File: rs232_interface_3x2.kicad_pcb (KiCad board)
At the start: 2 copper layers, 70.5 x 41.9 mm, 9 parts, among them J1 DB9M_RA, U1 RS232_2x2

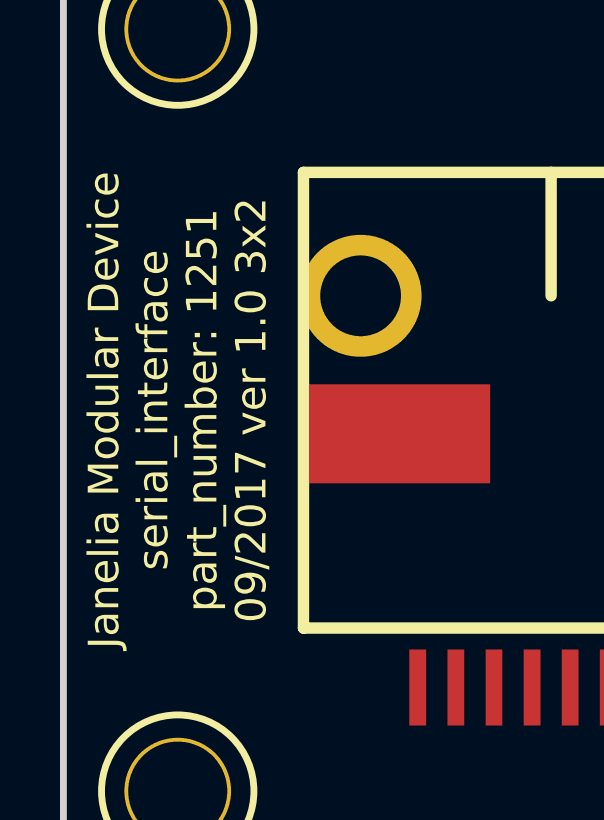
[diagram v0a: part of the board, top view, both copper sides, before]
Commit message: serial -> rs232.
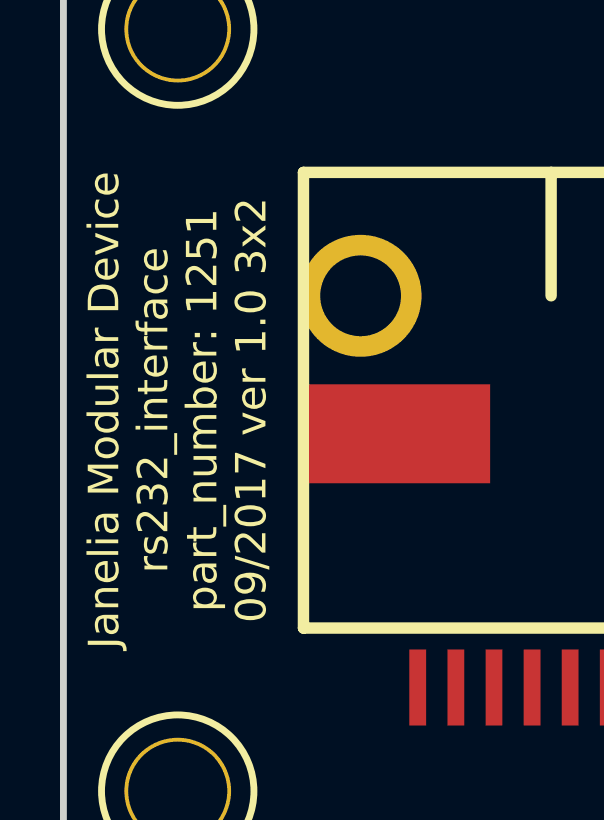
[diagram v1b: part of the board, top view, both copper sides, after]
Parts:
- C1, C2, C3, C4, C5: footprint serial_interface_3x2:SM1210 -> rs232_interface_3x2:SM1210
- J1: footprint serial_interface_3x2:DB9M_RA -> rs232_interface_3x2:DB9M_RA
- MDB1: footprint serial_interface_3x2:MODULAR_DEVICE_BASE_3X2_MALE -> rs232_interface_3x2:MODULAR_DEVICE_BASE_3X2_MALE
- RJ1: footprint serial_interface_3x2:RJ45_8P8C_2PORT_1ROW_RA_SMD -> rs232_interface_3x2:RJ45_8P8C_2PORT_1ROW_RA_SMD
- U1: footprint serial_interface_3x2:SOIC_16 -> rs232_interface_3x2:SOIC_16
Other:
- board text added: "Janelia Modular Device rs232_interface part_number: 1251 09/2017 ver 1.0 3x2"
- board text removed: "Janelia Modular Device serial_interface part_number: 1251 09/2017 ver 1.0 3x2"
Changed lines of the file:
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@@
   (page A4)
   (title_block
-    (title serial_interface_3x2)
+    (title rs232_interface_3x2)
     (rev 1.0)
   )
@@
     (diff_pair_width 0.254)
   )
-  (module serial_interface_3x2:DB9M_RA (layer F.Cu)
+  (module rs232_interface_3x2:DB9M_RA (layer F.Cu)
     (at 146.685 88.9 90)
     (fp_text reference J1 (at 0 -3.81 90) (layer F.SilkS)
@@
     (pad 9 thru_hole oval (at 4.155 1.42 90) (size 1.6 2.2) (drill 1) (layers *.Cu *.Mask))
   )
-  (module serial_interface_3x2:SOIC_16 (layer B.Cu)
+  (module rs232_interface_3x2:SOIC_16 (layer B.Cu)
     (at 134.62 88.9)
     (solder_mask_margin 0.1016)
@@
       (net 2 "Net-(C1-Pad1)"))
   )
-  (module serial_interface_3x2:MODULAR_DEVICE_BASE_3X2_MALE (layer F.Cu)
+  (module rs232_interface_3x2:MODULAR_DEVICE_BASE_3X2_MALE (layer F.Cu)
     (at 107.315 88.9)
     (fp_text reference MDB1 (at 0 0) (layer F.SilkS) hide
@@
       (net 6 GND))
   )
-  (module serial_interface_3x2:SM1210 (layer F.Cu)
+  (module rs232_interface_3x2:SM1210 (layer F.Cu)
     (at 169.181802 91.811719)
     (tags "CMS SM")
@@
     )
   )
-  (module serial_interface_3x2:SM1210 (layer F.Cu)
+  (module rs232_interface_3x2:SM1210 (layer F.Cu)
     (at 200.871802 85.101719)
     (tags "CMS SM")
@@
     )
   )
-  (module serial_interface_3x2:SM1210 (layer F.Cu)
+  (module rs232_interface_3x2:SM1210 (layer F.Cu)
     (at 174.381802 91.811719)
     (tags "CMS SM")
@@
     )
   )
-  (module serial_interface_3x2:SM1210 (layer F.Cu)
+  (module rs232_interface_3x2:SM1210 (layer F.Cu)
     (at 213.061802 70.911719)
     (tags "CMS SM")
@@
     )
   )
-  (module serial_interface_3x2:SM1210 (layer F.Cu)
+  (module rs232_interface_3x2:SM1210 (layer F.Cu)
     (at 179.581802 91.811719)
     (tags "CMS SM")
@@
     )
   )
-  (module serial_interface_3x2:RJ45_8P8C_2PORT_1ROW_RA_SMD (layer F.Cu)
+  (module rs232_interface_3x2:RJ45_8P8C_2PORT_1ROW_RA_SMD (layer F.Cu)
     (at 109.855 85.09 180)
     (fp_text reference RJ1 (at 0 -12.065 180) (layer F.SilkS)
@@
     (effects (font (size 1.016 1.016) (thickness 0.1905)))
   )
-  (gr_text "Janelia Modular Device\nserial_interface\npart_number: 1251\n09/2017 ver 1.0 3x2" (at 89.535 88.9 90) (layer F.SilkS)
+  (gr_text "Janelia Modular Device\nrs232_interface\npart_number: 1251\n09/2017 ver 1.0 3x2" (at 89.535 88.9 90) (layer F.SilkS)
     (effects (font (size 1.016 1.016) (thickness 0.254)))
   )

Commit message: Progress towards v1.0.
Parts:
- removed RJ1: RJ45_8P8C_2PORT_1ROW_RA_SMD, rs232_interface_3x2:RJ45_8P8C_2PORT_1ROW_RA_SMD
- added J2: DB9F, rs232_interface_3x2:DB9F, F.Cu at (109.9, 96.5)
- C1, C2, C3, C4, C5: moved to B.Cu
- J1: value DB9M_RA -> DB9M; footprint rs232_interface_3x2:DB9M_RA -> rs232_interface_3x2:DB9M
- moved C4 71.7 mm to (146.1, 96.5), turned to 270 degrees
- moved C2 55.2 mm to (146.1, 91.4), turned to 270 degrees
- moved C5 53.0 mm to (127.0, 85.1), turned to 270 degrees
- moved J1 37.6 mm to (109.9, 81.3), turned to 0 degrees
- moved C3 30.2 mm to (146.1, 81.3), turned to 90 degrees
- moved C1 23.8 mm to (146.1, 86.4), turned to 270 degrees
- moved U1 2.01 mm to (136.5, 88.3), turned to 180 degrees
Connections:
- net /RD renamed /RXD
- net /TD renamed /TXD
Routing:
- net GND: track 0.00 -> 110.0 mm
- net +3V3: track 0.00 -> 49.4 mm, vias 0 -> 1
- net /RXD: track 0.00 -> 42.8 mm
- net /TXD: track 0.00 -> 36.2 mm
- net /RX2: track 0.00 -> 29.4 mm
- net /TX2: track 0.00 -> 28.9 mm
- net Net-(C1-Pad1): track 0.00 -> 9.60 mm
- net Net-(C4-Pad1): track 0.00 -> 7.61 mm
- net Net-(C2-Pad2): track 0.00 -> 6.43 mm
- net Net-(C3-Pad1): track 0.00 -> 6.34 mm
- net Net-(C2-Pad1): track 0.00 -> 5.69 mm
- net Net-(C1-Pad2): track 0.00 -> 4.81 mm
- added copper zone on B.Cu, net GND
- added copper zone on F.Cu, net GND
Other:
- net class Default: trace_width 0.25 -> 0.254
- board text added: "2"
- board text added: "J1 MALE PINS DTE (PC) 2: RXD (DTE IN) <- TXD (DCE OUT) 3: TXD (DTE OUT) -> RXD (DCE IN) 5: GND"
- board text added: "J2 FEMALE SOCKETS DCE (PERIPHERAL) 2: TXD (DCE OUT) -> RXD (DTE IN) 3: RXD (DCE IN) <- TXD (DTE OUT) 5: GND"

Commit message: Finished v1.0.
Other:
- net class Default: trace_width 0.254 -> 0.25
- board text added: "Use D-SUB 9 M/F serial extension cable (not null modem) with either J1 or J2 (not both)."
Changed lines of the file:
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@@
-(kicad_pcb (version 20170123) (host pcbnew no-vcs-found-66b654f~60~ubuntu16.04.1)
+(kicad_pcb (version 20170123) (host pcbnew no-vcs-found-e2d3fce~60~ubuntu16.04.1)
   (general
     (thickness 1.6)
-    (drawings 9)
+    (drawings 10)
     (tracks 105)
     (zones 0)
@@
   )
   (setup
-    (last_trace_width 0.254)
+    (last_trace_width 0.25)
     (trace_clearance 0.0254)
     (zone_clearance 0.2032)
@@
   (net_class Default "This is the default net class."
     (clearance 0.0254)
-    (trace_width 0.254)
-    (via_dia 0.889)
-    (via_drill 0.635)
-    (uvia_dia 0.508)
-    (uvia_drill 0.127)
-    (diff_pair_gap 0.254)
-    (diff_pair_width 0.254)
+    (trace_width 0.25)
+    (via_dia 0.889)
+    (via_drill 0.635)
+    (uvia_dia 0.508)
+    (uvia_drill 0.127)
   )
   (net_class GND ""
@@
     (pad "" thru_hole oval (at -12.495 0) (size 5 6) (drill 3.1) (layers *.Cu *.Mask))
   )
+  (gr_text "Use D-SUB 9 M/F serial\nextension cable\n(not null modem)\nwith either J1 or J2\n(not both)." (at 133.985 105.41) (layer F.SilkS)
+    (effects (font (size 0.762 0.762) (thickness 0.1905)) (justify left))
+  )
   (gr_text 2 (at 154.305 88.9) (layer F.SilkS)
